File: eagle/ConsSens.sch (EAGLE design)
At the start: 31 parts, among them Q3 12MHz, U3 3.3V, X1 MINI-USB-SHIELD-UX60A-MB-5ST

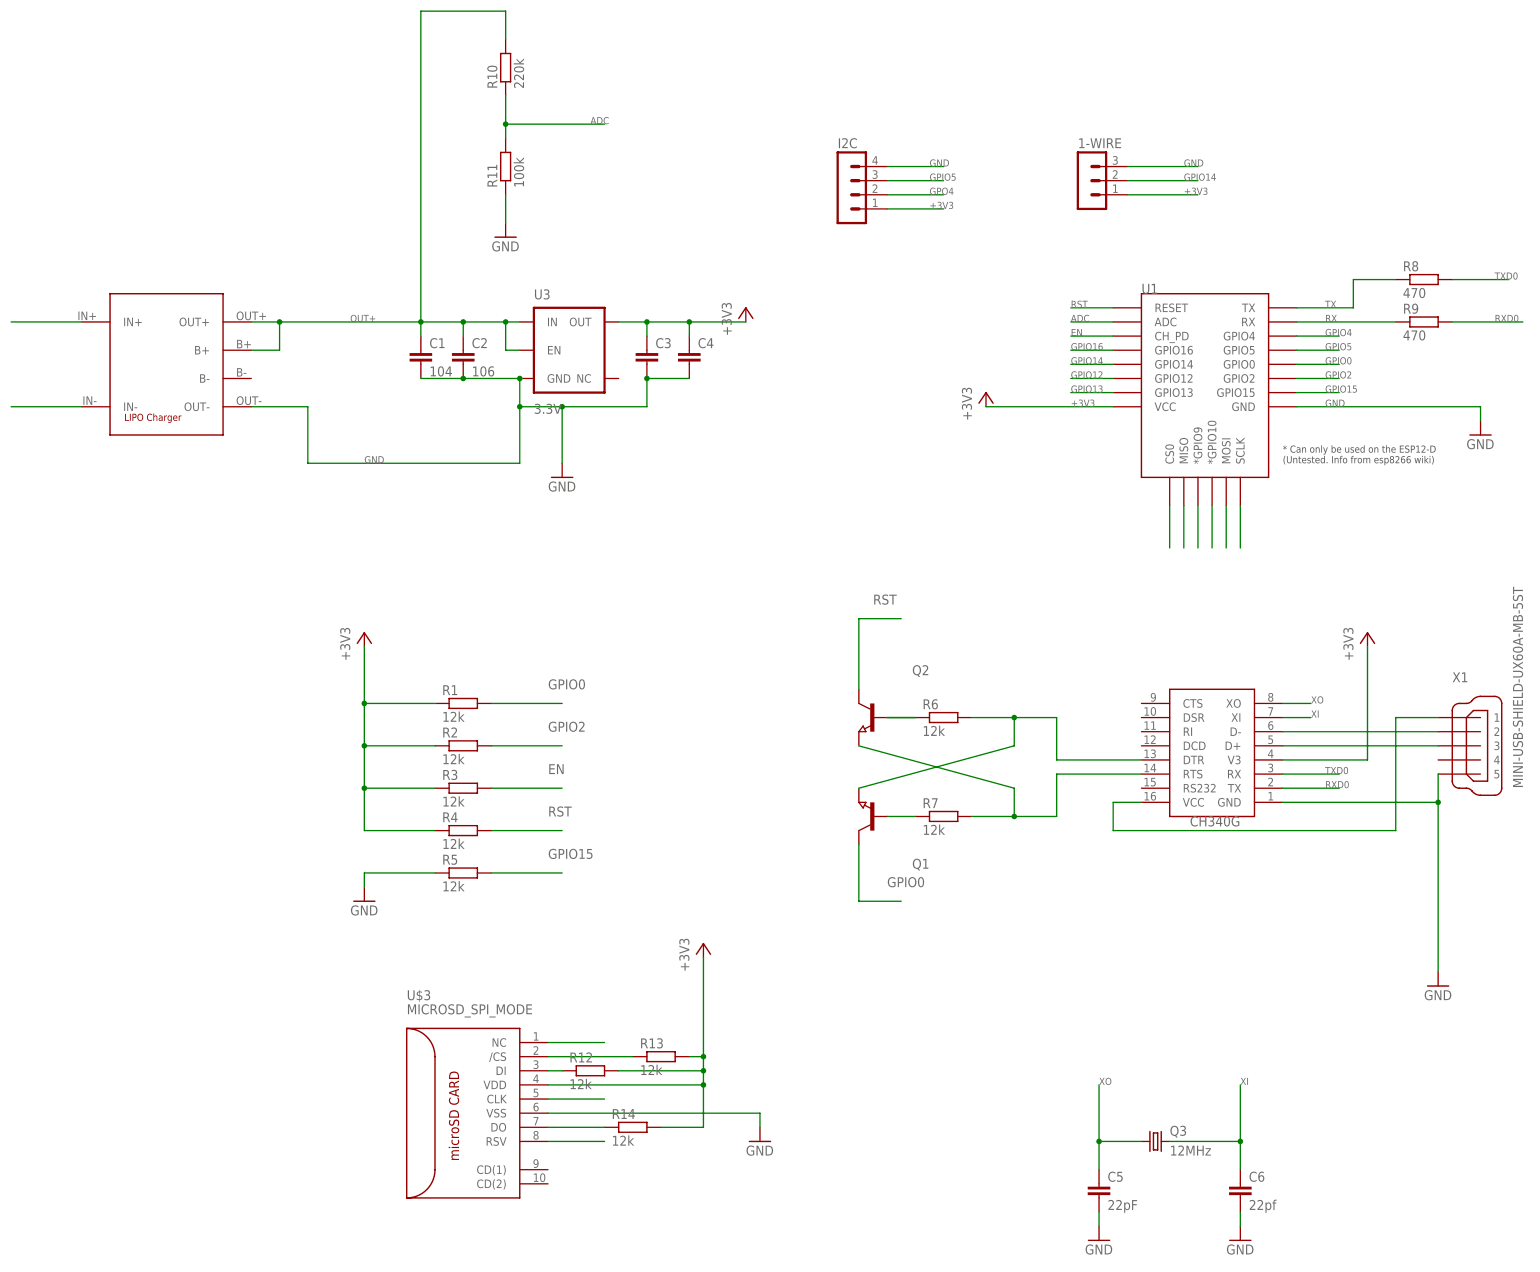
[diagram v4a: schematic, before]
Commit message: New Micro-USB Connector
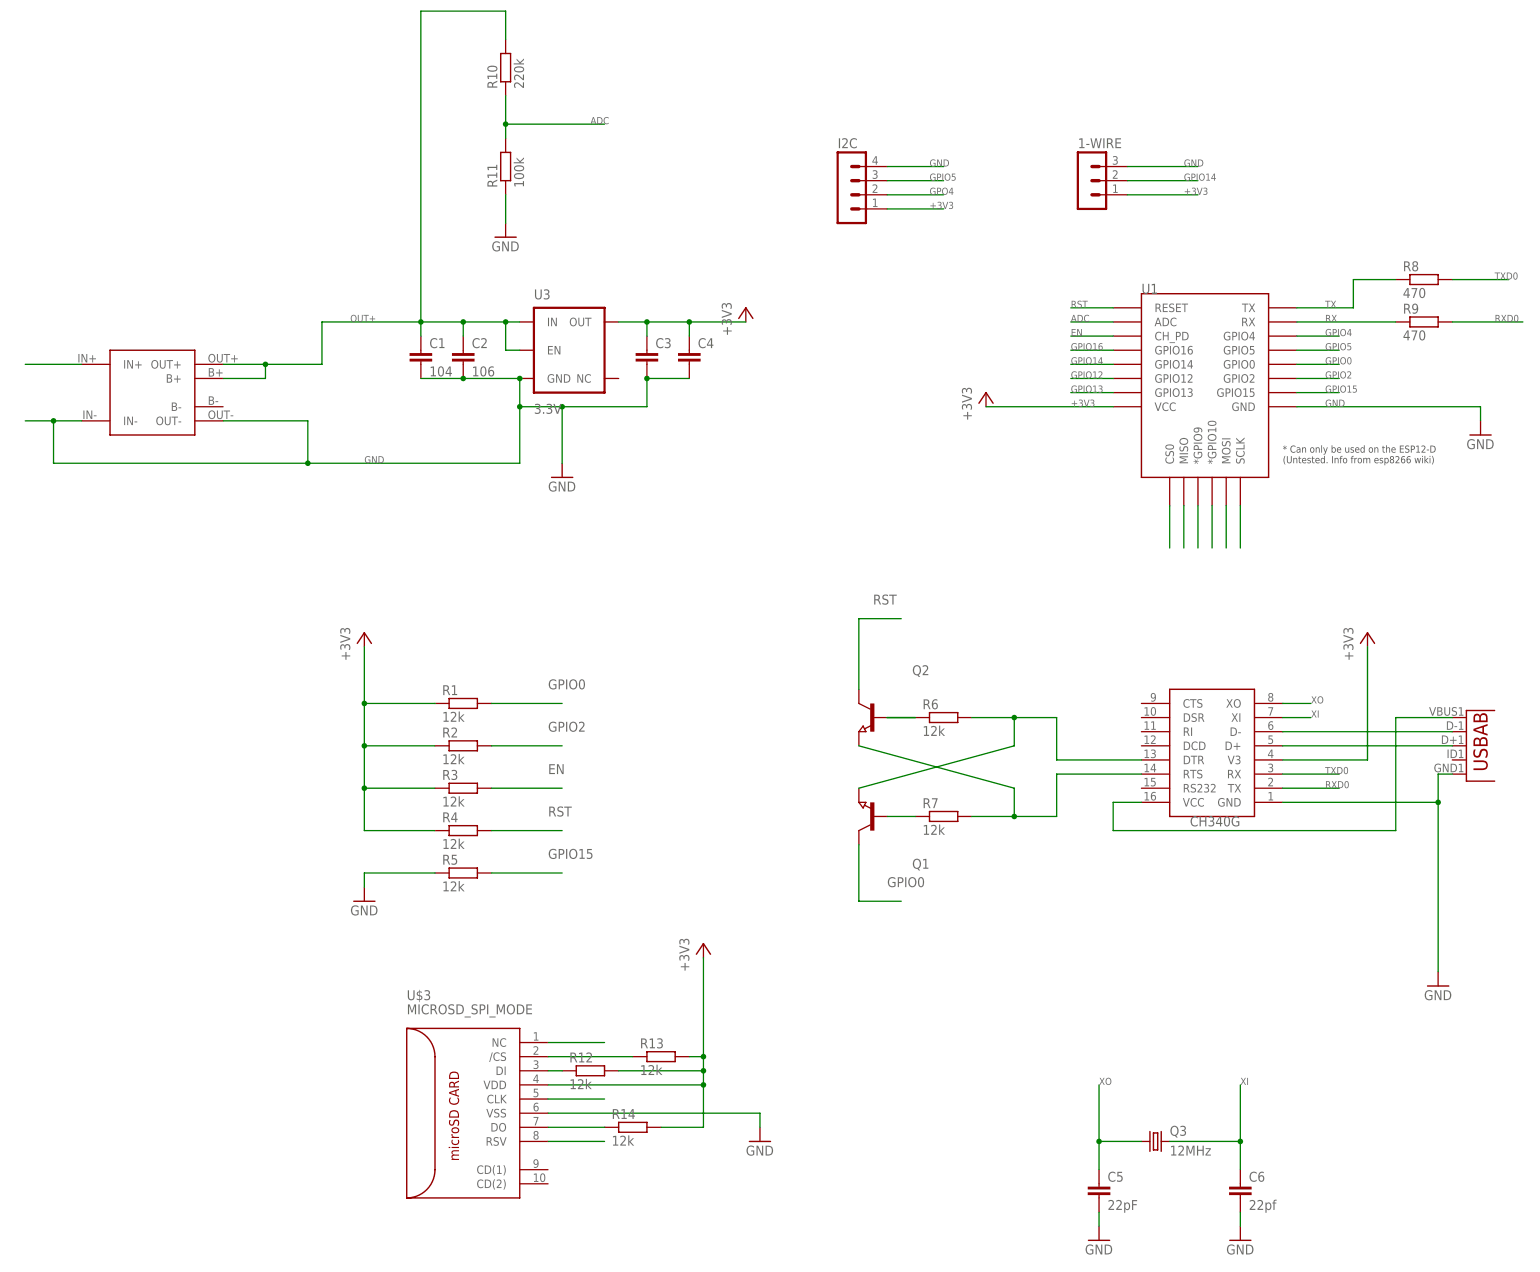
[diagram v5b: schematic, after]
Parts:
- removed U$2: LIPOCHARGER, aliexpress:LIPOCHARGER
- removed X1: MINI-USB-SHIELD-UX60A-MB-5ST, con-hirose:MINI-USB-SHIELD-UX60A-MB-5ST
- added MICROUSB: (no value), MicroUSB:USB""
- added U$4: TP4056-MODULE, userlib:TP4056-MODULE
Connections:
- net GND: now also MICROUSB.GND, U$4.IN-, U$4.OUT-; no longer U$2.IN-, U$2.OUT-, X1G$1.5
- net N$5: now also MICROUSB.D-; no longer X1G$1.2
- net N$6: now also MICROUSB.D+; no longer X1G$1.3
- net OUT+: now also U$4.B+, U$4.OUT+; no longer U$2.B+, U$2.OUT+
- net USB5V: now also MICROUSB.VBUS, U$4.IN+; no longer U$2.IN+, X1G$1.1
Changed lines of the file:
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@@
 <part name="R7" library="eagle-ltspice" deviceset="R" device="R0603" value="12k"/>
 <part name="U$1" library="ch340g" deviceset="CH340G" device=""/>
-<part name="X1" library="con-hirose" deviceset="MINI-USB-SHIELD-" device="UX60A-MB-5ST"/>
 <part name="GND3" library="supply1" deviceset="GND" device=""/>
 <part name="GND4" library="supply1" deviceset="GND" device=""/>
@@
 <part name="R11" library="eagle-ltspice" deviceset="R" device="R0603" value="100k"/>
 <part name="GND5" library="supply1" deviceset="GND" device=""/>
-<part name="U$2" library="aliexpress" deviceset="LIPOCHARGER" device=""/>
 <part name="Q3" library="SparkFun-FreqCtrl" deviceset="CRYSTAL" device="CRYSTAL-SMD-5X3-12MHZ" value="12MHz"/>
 <part name="GND6" library="supply1" deviceset="GND" device=""/>
@@
 <part name="I2C" library="con-lstb" deviceset="MA04-1" device=""/>
 <part name="1-WIRE" library="con-lstb" deviceset="MA03-1" device=""/>
+<part name="U$4" library="userlib" deviceset="TP4056-MODULE" device=""/>
+<part name="MICROUSB" library="MicroUSB" deviceset="USB" device="&quot;&quot;"/>
 </parts>
 <sheets>
@@
 <instance part="R7" gate="G$1" x="78.74" y="-2.54"/>
 <instance part="U$1" gate="G$1" x="127" y="10.16" rot="R180"/>
-<instance part="X1" gate="G$1" x="172.72" y="10.16"/>
 <instance part="GND3" gate="1" x="175.26" y="66.04"/>
 <instance part="GND4" gate="1" x="167.64" y="-33.02"/>
@@
 <instance part="R11" gate="G$1" x="0" y="114.3" rot="R90"/>
 <instance part="GND5" gate="1" x="0" y="101.6"/>
-<instance part="U$2" gate="G$1" x="-63.5" y="78.74"/>
 <instance part="Q3" gate="G$1" x="116.84" y="-60.96"/>
 <instance part="GND6" gate="1" x="106.68" y="-78.74"/>
@@
 <instance part="I2C" gate="1" x="60.96" y="111.76"/>
 <instance part="1-WIRE" gate="G$1" x="104.14" y="111.76"/>
+<instance part="U$4" gate="G$1" x="-63.5" y="73.66"/>
+<instance part="MICROUSB" gate="G$1" x="175.26" y="10.16" rot="MR180"/>
 </instances>
 <busses>
@@
 <junction x="2.54" y="71.12"/>
 <label x="-25.4" y="60.96" size="1.27" layer="95"/>
-<pinref part="U$2" gate="G$1" pin="OUT-"/>
-<wire x1="-45.72" y1="71.12" x2="-35.56" y2="71.12" width="0.1524" layer="91"/>
-<wire x1="-35.56" y1="71.12" x2="-35.56" y2="60.96" width="0.1524" layer="91"/>
+<wire x1="-35.56" y1="68.58" x2="-35.56" y2="60.96" width="0.1524" layer="91"/>
+<pinref part="U$4" gate="G$1" pin="OUT-"/>
+<wire x1="-50.8" y1="68.58" x2="-35.56" y2="68.58" width="0.1524" layer="91"/>
+<pinref part="U$4" gate="G$1" pin="IN-"/>
+<wire x1="-76.2" y1="68.58" x2="-81.28" y2="68.58" width="0.1524" layer="91"/>
+<wire x1="-81.28" y1="68.58" x2="-86.36" y2="68.58" width="0.1524" layer="91"/>
+<wire x1="-81.28" y1="68.58" x2="-81.28" y2="60.96" width="0.1524" layer="91"/>
+<junction x="-81.28" y="68.58"/>
+<wire x1="-35.56" y1="60.96" x2="-81.28" y2="60.96" width="0.1524" layer="91"/>
+<junction x="-35.56" y="60.96"/>
 </segment>
 <segment>
@@
 <segment>
 <pinref part="GND4" gate="1" pin="GND"/>
-<pinref part="X1" gate="G$1" pin="5"/>
 <pinref part="U$1" gate="G$1" pin="GND"/>
 <wire x1="167.64" y1="-30.48" x2="167.64" y2="0" width="0.1524" layer="91"/>
@@
 <wire x1="139.7" y1="0" x2="167.64" y2="0" width="0.1524" layer="91"/>
 <junction x="167.64" y="0"/>
+<pinref part="MICROUSB" gate="G$1" pin="GND"/>
+<wire x1="167.64" y1="5.08" x2="170.18" y2="5.08" width="0.1524" layer="91"/>
 </segment>
 <segment>
@@
 <pinref part="R11" gate="G$1" pin="1"/>
 <wire x1="0" y1="104.14" x2="0" y2="109.22" width="0.1524" layer="91"/>
-</segment>
-<segment>
-<pinref part="U$2" gate="G$1" pin="IN-"/>
-<wire x1="-76.2" y1="71.12" x2="-88.9" y2="71.12" width="0.1524" layer="91"/>
 </segment>
 <segment>
@@
 <net name="N$5" class="0">
 <segment>
-<pinref part="X1" gate="G$1" pin="2"/>
 <pinref part="U$1" gate="G$1" pin="D-"/>
-<wire x1="167.64" y1="12.7" x2="139.7" y2="12.7" width="0.1524" layer="91"/>
+<wire x1="170.18" y1="12.7" x2="139.7" y2="12.7" width="0.1524" layer="91"/>
+<pinref part="MICROUSB" gate="G$1" pin="D-"/>
 </segment>
 </net>
@@
 <segment>
 <pinref part="U$1" gate="G$1" pin="D+"/>
-<pinref part="X1" gate="G$1" pin="3"/>
-<wire x1="139.7" y1="10.16" x2="167.64" y2="10.16" width="0.1524" layer="91"/>
+<wire x1="139.7" y1="10.16" x2="170.18" y2="10.16" width="0.1524" layer="91"/>
+<pinref part="MICROUSB" gate="G$1" pin="D+"/>
 </segment>
 </net>
@@
 <net name="USB5V" class="0">
 <segment>
-<pinref part="X1" gate="G$1" pin="1"/>
-<wire x1="167.64" y1="15.24" x2="160.02" y2="15.24" width="0.1524" layer="91"/>
+<wire x1="170.18" y1="15.24" x2="160.02" y2="15.24" width="0.1524" layer="91"/>
 <wire x1="160.02" y1="15.24" x2="160.02" y2="-5.08" width="0.1524" layer="91"/>
 <wire x1="160.02" y1="-5.08" x2="109.22" y2="-5.08" width="0.1524" layer="91"/>
@@
 <pinref part="U$1" gate="G$1" pin="VCC"/>
 <wire x1="109.22" y1="0" x2="114.3" y2="0" width="0.1524" layer="91"/>
-</segment>
-<segment>
-<pinref part="U$2" gate="G$1" pin="IN+"/>
-<wire x1="-76.2" y1="86.36" x2="-88.9" y2="86.36" width="0.1524" layer="91"/>
+<pinref part="MICROUSB" gate="G$1" pin="VBUS"/>
+</segment>
+<segment>
+<pinref part="U$4" gate="G$1" pin="IN+"/>
+<wire x1="-76.2" y1="78.74" x2="-86.36" y2="78.74" width="0.1524" layer="91"/>
 </segment>
 </net>
@@
 <wire x1="0" y1="86.36" x2="-7.62" y2="86.36" width="0.1524" layer="91"/>
 <wire x1="-7.62" y1="86.36" x2="-15.24" y2="86.36" width="0.1524" layer="91"/>
-<wire x1="-15.24" y1="86.36" x2="-40.64" y2="86.36" width="0.1524" layer="91"/>
-<wire x1="-40.64" y1="86.36" x2="-45.72" y2="86.36" width="0.1524" layer="91"/>
+<wire x1="-15.24" y1="86.36" x2="-33.02" y2="86.36" width="0.1524" layer="91"/>
 <wire x1="-15.24" y1="83.82" x2="-15.24" y2="86.36" width="0.1524" layer="91"/>
 <junction x="-15.24" y="86.36"/>
@@
 <wire x1="-15.24" y1="142.24" x2="-15.24" y2="86.36" width="0.1524" layer="91"/>
 <label x="-27.94" y="86.36" size="1.27" layer="95"/>
-<pinref part="U$2" gate="G$1" pin="OUT+"/>
-<pinref part="U$2" gate="G$1" pin="B+"/>
-<wire x1="-45.72" y1="81.28" x2="-40.64" y2="81.28" width="0.1524" layer="91"/>
-<wire x1="-40.64" y1="81.28" x2="-40.64" y2="86.36" width="0.1524" layer="91"/>
-<junction x="-40.64" y="86.36"/>
 <pinref part="U3" gate="G$1" pin="EN"/>
 <wire x1="2.54" y1="81.28" x2="0" y2="81.28" width="0.1524" layer="91"/>
 <wire x1="0" y1="81.28" x2="0" y2="86.36" width="0.1524" layer="91"/>
 <junction x="0" y="86.36"/>
+<pinref part="U$4" gate="G$1" pin="B+"/>
+<wire x1="-50.8" y1="76.2" x2="-43.18" y2="76.2" width="0.1524" layer="91"/>
+<wire x1="-43.18" y1="76.2" x2="-43.18" y2="78.74" width="0.1524" layer="91"/>
+<pinref part="U$4" gate="G$1" pin="OUT+"/>
+<wire x1="-43.18" y1="78.74" x2="-50.8" y2="78.74" width="0.1524" layer="91"/>
+<wire x1="-43.18" y1="78.74" x2="-33.02" y2="78.74" width="0.1524" layer="91"/>
+<wire x1="-33.02" y1="78.74" x2="-33.02" y2="86.36" width="0.1524" layer="91"/>
+<junction x="-43.18" y="78.74"/>
 </segment>
 </net>
@@
 </sheet>
 </sheets>
+<errors>
+</errors>
 </schematic>
 </drawing>
